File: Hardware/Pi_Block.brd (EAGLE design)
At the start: 30.5 x 87.6 mm, 52 parts, among them Q1 BSS138, U1 PCA9306, U2 EDISON_CONNECTOR_FULLMOUNTING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, U3 EDISON_CONNECTOR_FULLHEADER, U4 TPS62065, U5 MIC5219 3.3V, U6 TXB0108, U7 TXB0108

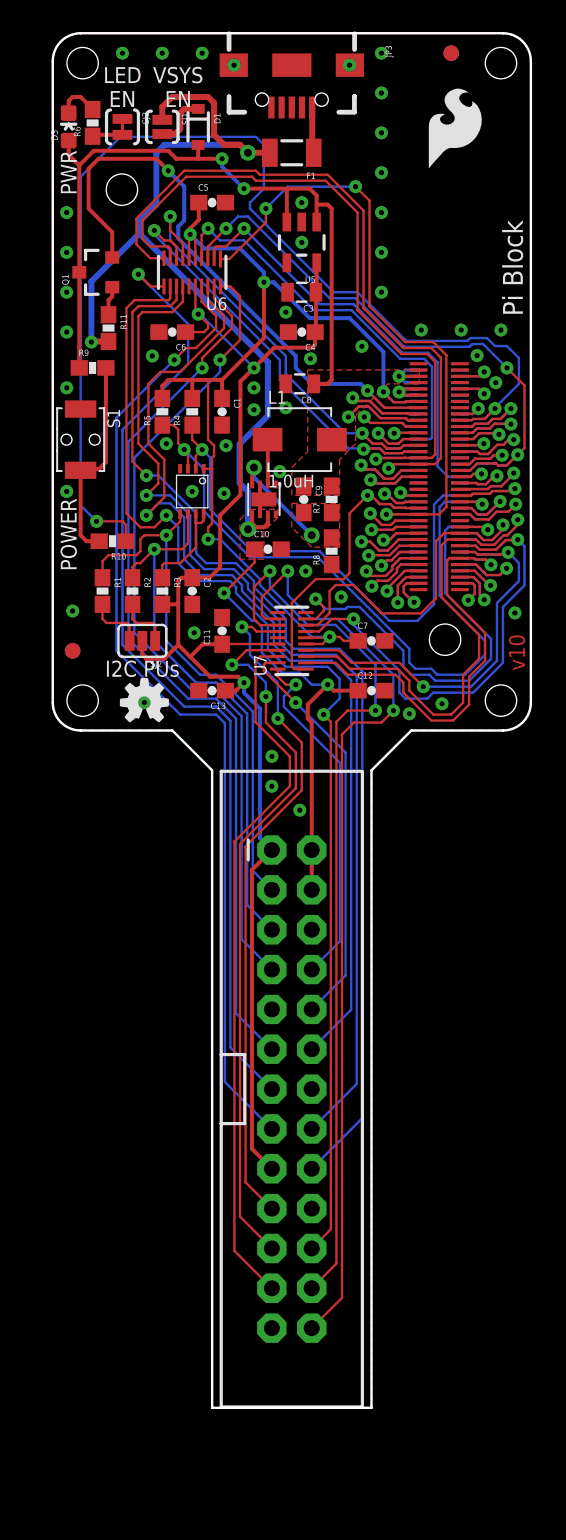
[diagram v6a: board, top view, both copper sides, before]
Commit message: Added ICs to SF lib. Added pin markers to ICs. Changed routing of TXB and PCA to come straight out pins. Added mounting hole below header. Added notes to board.
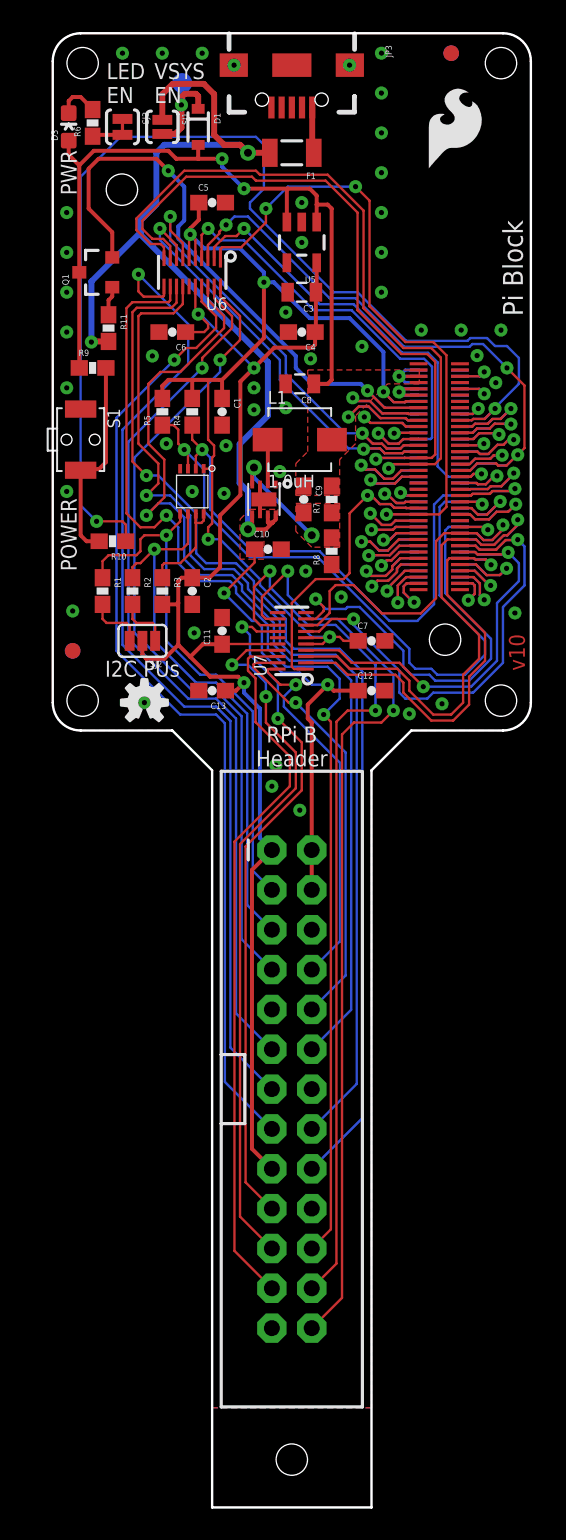
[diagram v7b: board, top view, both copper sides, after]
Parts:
- added FRAME3: FRAME-LETTER, SparkFun-Aesthetics:CREATIVE_COMMONS
- added TP1: TEST-POINT3X5, SparkFun-Passives:PAD.03X.05
- Q1: value BSS138 -> 200mA/50V
- U4: device Testing:WSON-8-PAD -> SparkFun-PowerIC:WSON-8-PAD
- U6, U7: device Testing:UFDFN-20 -> SparkFun-DigitalIC:UFDFN-20
- moved FRAME1 6.35 mm to (-1.27, -58.4)
- moved FRAME2 6.35 mm to (-1.27, -58.4)
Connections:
- net 1.8V: now also U6.5, U6.6, U7.5, U7.6; no longer U6.P$5, U6.P$6, U7.P$5, U7.P$6
- net 3.3V_LOCAL: now also U6.16, U7.16; no longer U6.P$16, U7.P$16
- net GND: now also U6.15, U7.15; no longer U6.P$15, U7.P$15
- net GP109_SPI_2_CLK: now also U7.3; no longer U7.P$3
- net GP110_SPI_2_FS0: now also U7.8; no longer U7.P$8
- net GP111_SPI_2_FS1: now also U7.9; no longer U7.P$9
- net GP114_SPI_2_RXD: now also U7.4; no longer U7.P$4
- net GP115_SPI_2_TXD: now also U7.7; no longer U7.P$7
- net GP12_PWM0: now also U6.2; no longer U6.P$2
- net GP130_UART_1_RX: now also U7.2; no longer U7.P$2
- net GP131_UART_1_TX: now also U7.1; no longer U7.P$1
- net GP13_PWM1: now also U6.3; no longer U6.P$3
- net GP14: now also U6.1; no longer U6.P$1
- net GP44: now also U6.4; no longer U6.P$4
- net GP45: now also U6.7; no longer U6.P$7
- net GP46: now also U6.8; no longer U6.P$8
- net GP47: now also U6.9; no longer U6.P$9
- net GP48: now also U6.10; no longer U6.P$10
- net N$3: now also TP1.P$1
- net PI_CE0: now also U7.13; no longer U7.P$13
- net PI_CE1: now also U7.12; no longer U7.P$12
- net PI_GP17: now also U6.19; no longer U6.P$19
- net PI_GP18#: now also U6.18; no longer U6.P$18
- net PI_GP22: now also U6.17; no longer U6.P$17
- net PI_GP23: now also U6.14; no longer U6.P$14
- net PI_GP24: now also U6.13; no longer U6.P$13
- net PI_GP25: now also U6.12; no longer U6.P$12
- net PI_GP27: now also U6.11; no longer U6.P$11
- net PI_GP4: now also U6.20; no longer U6.P$20
- net PI_MISO: now also U7.17; no longer U7.P$17
- net PI_MOSI: now also U7.14; no longer U7.P$14
- net PI_RXI: now also U7.19; no longer U7.P$19
- net PI_SCLK: now also U7.18; no longer U7.P$18
- net PI_TXO: now also U7.20; no longer U7.P$20
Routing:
- net N$3: track 3.54 -> 7.18 mm, vias 0 -> 1
- net 5V: track 86.8 -> 90.2 mm
- net PI_GP27: track 62.1 -> 63.6 mm
- net PI_RXI: track 26.0 -> 27.2 mm
- net PI_TXO: track 22.6 -> 23.6 mm
- net PI_SCLK: track 44.9 -> 45.6 mm
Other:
- board size 30.5 x 87.6 mm -> 30.5 x 94 mm
- board text added: "NOTES: - Board thickness = 0.063 in."
- board text added: "RPi B Header"
